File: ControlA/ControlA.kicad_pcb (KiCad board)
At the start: 2 copper layers, 164 parts, among them CN1 PH-4A_RHOS, J1 XT30PW-M, J2 Conn_01x08, J3 Conn_01x06, J4 Conn_01x03, Q1 HSBA15810C, Q2 HSBA15810C, Q3 HSBA15810C, Q4 HSBA15810C, Q5 HSBA15810C, Q6 HSBA15810C, SW1 TS-KG87S-AT15F, U1 XH-2PWBPZ, U10 YSPI0530-220M, U2 AMS1117-3.3, U3 STM32F405RGTx, U4 DRV8302DCAR, U5 ESDCAN24-2BLY, U6 744227S, U7 SN65HVD230D, U8 B06B-PARK-1_(LF)(SN), U9 TYPE-C_16PIN_2MD(073), Y1 Crystal

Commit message: start placement compentent
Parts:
- Q3: value HSBA15810C -> MOSFET
- moved C47 469.2 mm to (45.5, 103.0)
- moved C38 456.1 mm to (53.5, 111.5)
- moved C45 450.5 mm to (64.5, 92.0)
- moved C44 450.5 mm to (64.5, 89.0)
- moved C48 446.8 mm to (67.5, 116.5)
- moved C46 446.6 mm to (67.5, 113.5)
- moved C40 446.1 mm to (64.5, 94.5)
- moved C36 442.6 mm to (46.0, 106.0)
- moved C42 441.1 mm to (70.0, 95.0)
- moved C41 441.0 mm to (70.0, 92.5)
- moved C43 440.9 mm to (70.0, 100.4), turned to -90 degrees
- moved C34 439.1 mm to (49.5, 93.0)
- moved C35 439.1 mm to (49.5, 96.0)
- moved C39 435.7 mm to (74.6, 98.0), turned to 180 degrees
- moved C32 435.4 mm to (53.5, 105.5)
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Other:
- board text added: "CAN"
- board text added: "FILTRE"
- board text added: "INPUT PROTECTION"
- board text added: "MCU"
- board text added: "MOSFET DRIVER"
- board text added: "STEP DOWN CONVERT"
- board text added: "USB"

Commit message: CHANGE V11
change v1
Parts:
- C10, C11, C12, C26, C27, C28, C29, C30, C31, C32, C33, C34, C35, C36, C37, C38, C39, C4, C40, C41, C42, C43, C44, C45, C46, C47, C48, C5, C52, C53, C54, C55, C56, C57, C58, C59, C6, C60, C61, C62, C7, C8, C9: footprint Capacitor_SMD:C_0805_2012Metric -> Capacitor_SMD:C_0603_1608Metric
- C2, C3: moved to B.Cu
- Q3: value MOSFET -> HSBA15810C
- moved C54 191.5 mm to (77.4, 78.3)
- moved CN1 190.0 mm to (54.4, 105.4)
- moved U7 187.5 mm to (82.0, 99.8)
- moved R37 187.3 mm to (63.6, 100.9)
- moved R40 185.9 mm to (83.5, 78.7)
- moved U6 185.9 mm to (71.5, 99.0)
- moved C53 185.0 mm to (61.6, 94.2)
- moved C52 183.1 mm to (64.3, 106.0)
- moved R38 183.1 mm to (67.6, 104.0)
- moved U5 183.0 mm to (63.2, 97.2)
- moved R39 182.7 mm to (63.5, 81.0)
- moved C24 174.8 mm to (110.8, 62.6)
- moved R15 174.8 mm to (109.3, 64.7)
- moved Y1 171.2 mm to (87.1, 75.3)
- moved C11 170.5 mm to (90.8, 76.7)
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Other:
- board outline added: 100 x 78.8 mm
- board text removed: "CAN"
- board text removed: "FILTRE"
- board text removed: "INPUT PROTECTION"
- board text removed: "MCU"
- board text removed: "MOSFET DRIVER"
- board text removed: "STEP DOWN CONVERT"
- board text removed: "USB"

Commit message: connector
add conctor power mosft
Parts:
- added J5: Conn_01x01, footprint:7461097, F.Cu at (155.0, 76.4)
- added J6: Conn_01x01, footprint:7461097, F.Cu at (155.0, 89.5)
- added J7: Conn_01x01, footprint:7461097, F.Cu at (155.0, 102.7)
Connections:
- Q3 pad 4: /MOSFTs/M_H2_RG -> +VDC
- R60 pad 2: /MOSFTs/M_H2_RG -> +VDC
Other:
- board size 100 x 78.8 mm -> 111.6 x 78.8 mm

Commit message: net change
change net
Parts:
- moved C10 146.8 mm to (243.3, 106.9)
- moved C11 146.8 mm to (237.5, 79.3)
- moved C14 146.8 mm to (252.2, 102.2)
- moved C15 146.8 mm to (241.9, 87.0)
- moved C17 146.8 mm to (249.2, 86.2)
- moved C18 146.8 mm to (271.9, 79.9)
- moved C19 146.8 mm to (258.2, 102.5)
- moved C21 146.8 mm to (229.0, 73.7)
- moved C22 146.8 mm to (244.4, 84.5)
- moved C23 146.8 mm to (241.4, 84.5)
- moved C24 146.8 mm to (257.5, 65.2)
- moved C9 146.8 mm to (233.9, 86.1)
- moved D6 146.8 mm to (253.8, 76.7)
- moved D7 146.8 mm to (236.4, 113.4)
- moved D8 146.8 mm to (239.9, 113.4)
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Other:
- copper layers 2 -> 4
- rule pad_to_mask_clearance: 0 -> 0.08

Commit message: layout
layout mcu
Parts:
- R10, R11: footprint Resistor_SMD:R_0805_2012Metric -> Resistor_SMD:R_0402_1005Metric
- moved C13 179.7 mm to (92.0, 74.5), turned to 0 degrees
- moved C18 179.5 mm to (92.5, 73.0)
- moved R9 164.6 mm to (88.9, 71.0)
- moved D6 164.0 mm to (90.0, 68.0)
- moved C20 160.5 mm to (82.5, 84.0)
- moved R15 160.1 mm to (96.0, 72.0), turned to 90 degrees
- moved C24 159.7 mm to (98.0, 72.0), turned to -90 degrees
- moved C19 159.6 mm to (99.0, 91.0)
- moved C14 159.1 mm to (93.5, 91.0)
- moved C25 158.8 mm to (89.0, 94.9), turned to 0 degrees
- moved R16 158.6 mm to (91.0, 91.9)
- moved SDNT2012X103F3950FTF2 158.6 mm to (88.5, 91.9)
- moved FB1 157.6 mm to (85.0, 86.0), turned to -90 degrees
- moved C10 157.6 mm to (89.0, 75.0), turned to 90 degrees
- moved C11 156.5 mm to (81.0, 79.0), turned to 180 degrees
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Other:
- outline, holes or cut-outs redrawn

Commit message: update
update layout
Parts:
- moved C33 77.9 mm to (193.6, 70.0)
- moved C36 67.7 mm to (107.6, 80.0), turned to 90 degrees
- moved D14 50.9 mm to (143.5, 67.3), turned to -90 degrees
- moved D10 43.4 mm to (131.1, 71.8), turned to 0 degrees
- moved C31 43.2 mm to (131.4, 66.0), turned to 180 degrees
- moved R18 43.2 mm to (140.8, 76.2)
- moved U10 41.9 mm to (137.4, 69.6), turned to -90 degrees
- moved C30 41.8 mm to (131.3, 69.4), turned to 180 degrees
- moved R31 40.3 mm to (135.0, 78.9)
- moved C39 40.2 mm to (131.4, 67.7)
- moved C2 36.1 mm to (171.7, 64.0)
- moved C3 36.1 mm to (169.9, 79.8)
- moved C4 36.1 mm to (181.4, 115.7)
- moved C60 36.1 mm to (166.6, 98.8)
- moved C61 36.1 mm to (166.4, 117.0)
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
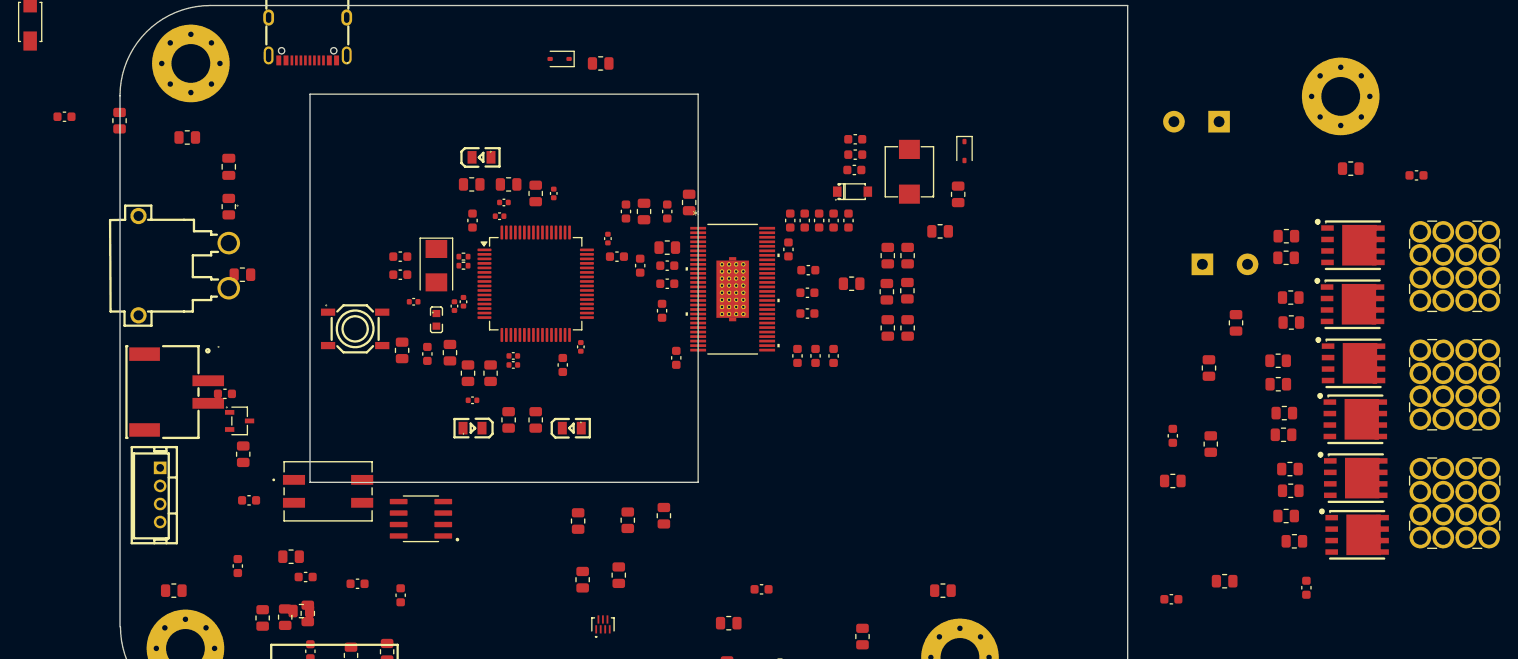
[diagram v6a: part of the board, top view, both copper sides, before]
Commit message: upta new layer
updute new layer cheek  cpaictor  change from bttom side to front
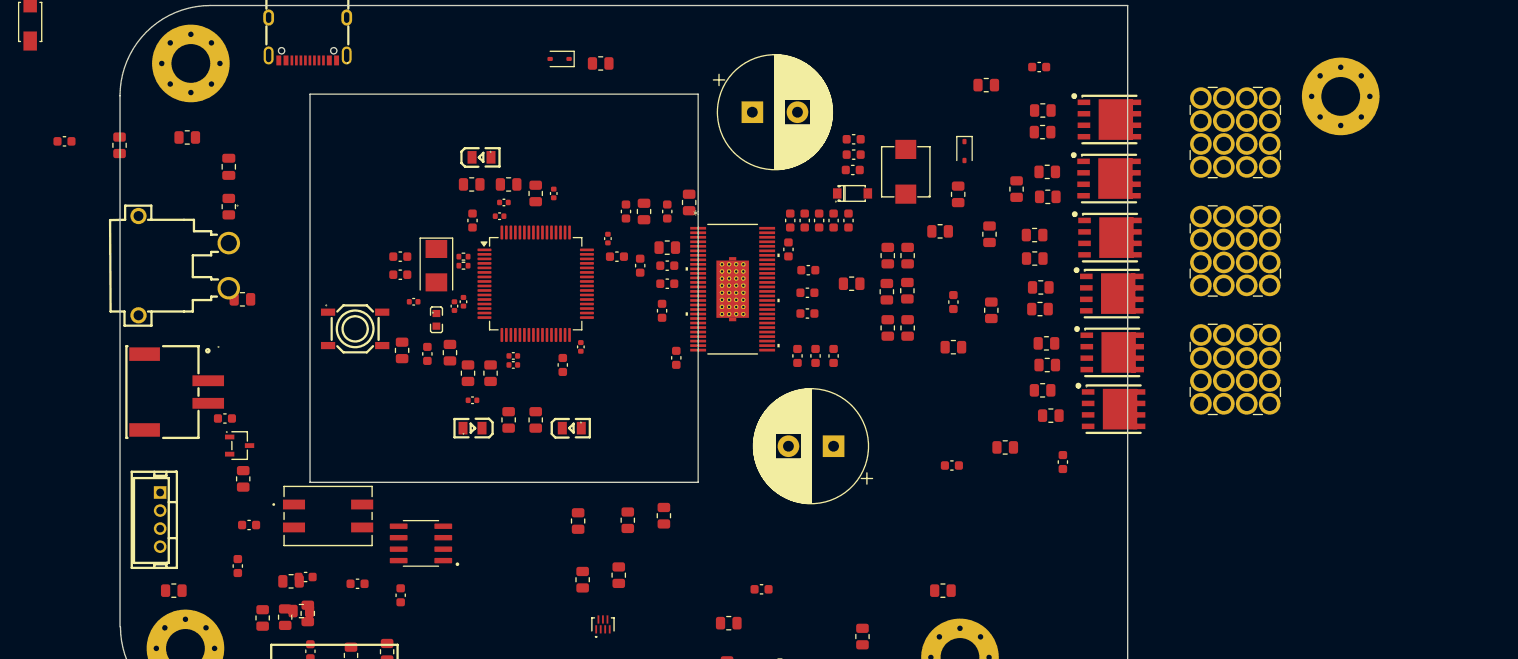
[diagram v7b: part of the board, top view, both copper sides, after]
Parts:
- C2, C3: moved to F.Cu
- moved C2 51.7 mm to (120.0, 63.0), turned to 0 degrees
- moved C3 45.6 mm to (129.0, 100.0), turned to 180 degrees
- moved C33 43.5 mm to (151.8, 58.0)
- moved R70 41.4 mm to (145.9, 60.0)
- moved Q2 30.4 mm to (159.5, 70.3)
- moved Q4 30.4 mm to (159.8, 83.1)
- moved R58 30.4 mm to (152.7, 72.4)
- moved R67 30.4 mm to (152.2, 93.8)
- moved C4 30.4 mm to (154.4, 101.8)
- moved Q1 30.4 mm to (159.6, 63.8)
- moved Q3 30.4 mm to (159.6, 76.9)
- moved Q5 30.4 mm to (159.9, 89.6)
- moved Q6 30.4 mm to (160.0, 95.9)
- moved R54 30.4 mm to (152.2, 62.8)
- moved R56 30.4 mm to (152.1, 65.2)
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
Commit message: change in shama
change schema and lyout
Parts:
- moved C61 9.83 mm to (135.9, 94.5)
- moved C4 9.52 mm to (145.9, 97.5)
- moved R64 9.07 mm to (141.8, 93.5)
- moved R70 7.93 mm to (138.8, 56.5)
- moved SW1 6.08 mm to (70.0, 88.0)
- moved R4 5.51 mm to (136.8, 88.5)
- moved C3 5.15 mm to (125.2, 96.5)
- moved R48 4.96 mm to (142.9, 81.5)
- moved C10 4.47 mm to (85.0, 73.0)
- moved C11 4.47 mm to (77.0, 77.0)
- moved C12 4.47 mm to (77.0, 79.0)
- moved C13 4.47 mm to (88.0, 72.5)
- moved C14 4.47 mm to (89.5, 89.0)
- moved C15 4.47 mm to (89.5, 88.0)
- moved C16 4.47 mm to (97.0, 87.0)
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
